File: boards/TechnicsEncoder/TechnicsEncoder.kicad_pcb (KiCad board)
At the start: 2 copper layers, 110.5 x 52.6 mm, 32 parts, among them J1 ISP, J2 Bender, J3 Technics, J4 SelectRX, J5 MIDI In, J6 MIDI Out, J7 BoardCon, J8 PistonEncoder, U1 ATmega48-20P, U2 6N137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

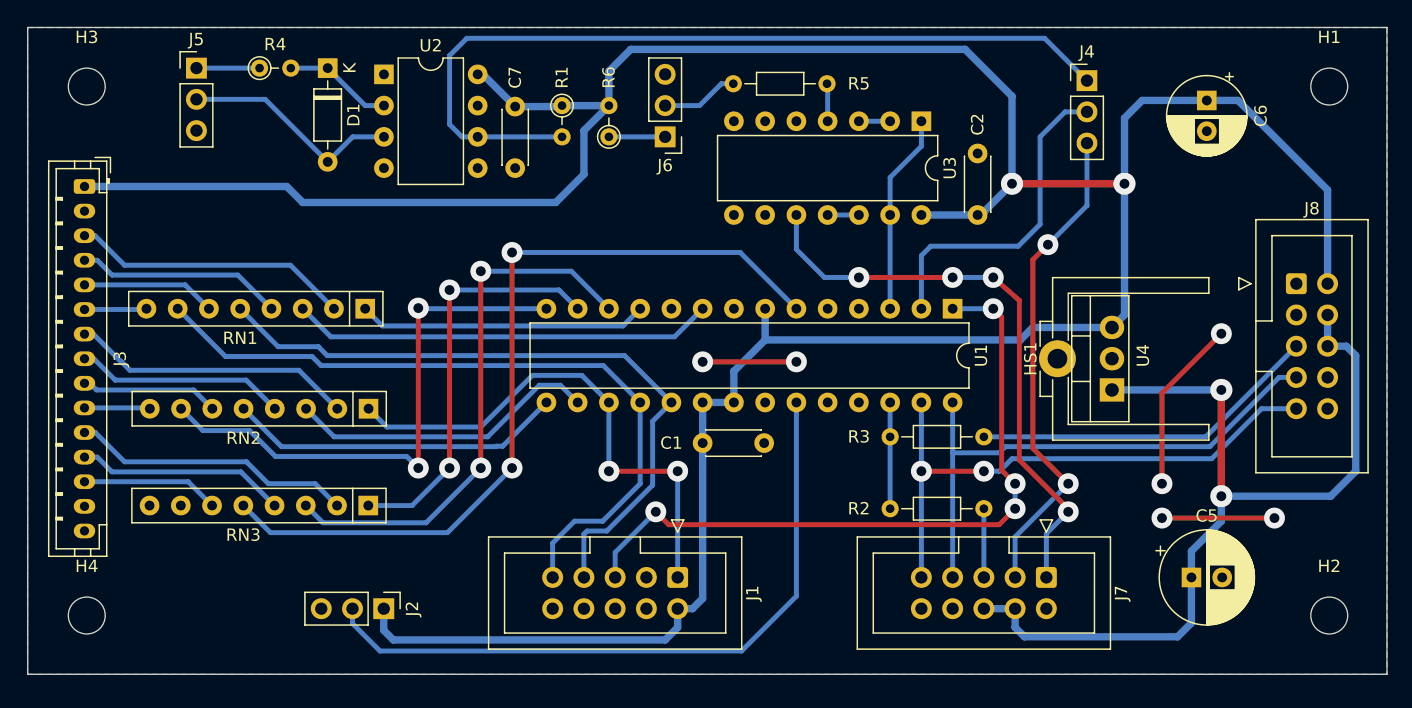
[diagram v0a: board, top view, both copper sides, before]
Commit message: Cleanup of PCB sizes and mounthole positions. Moved MIDI connectors to separate board.
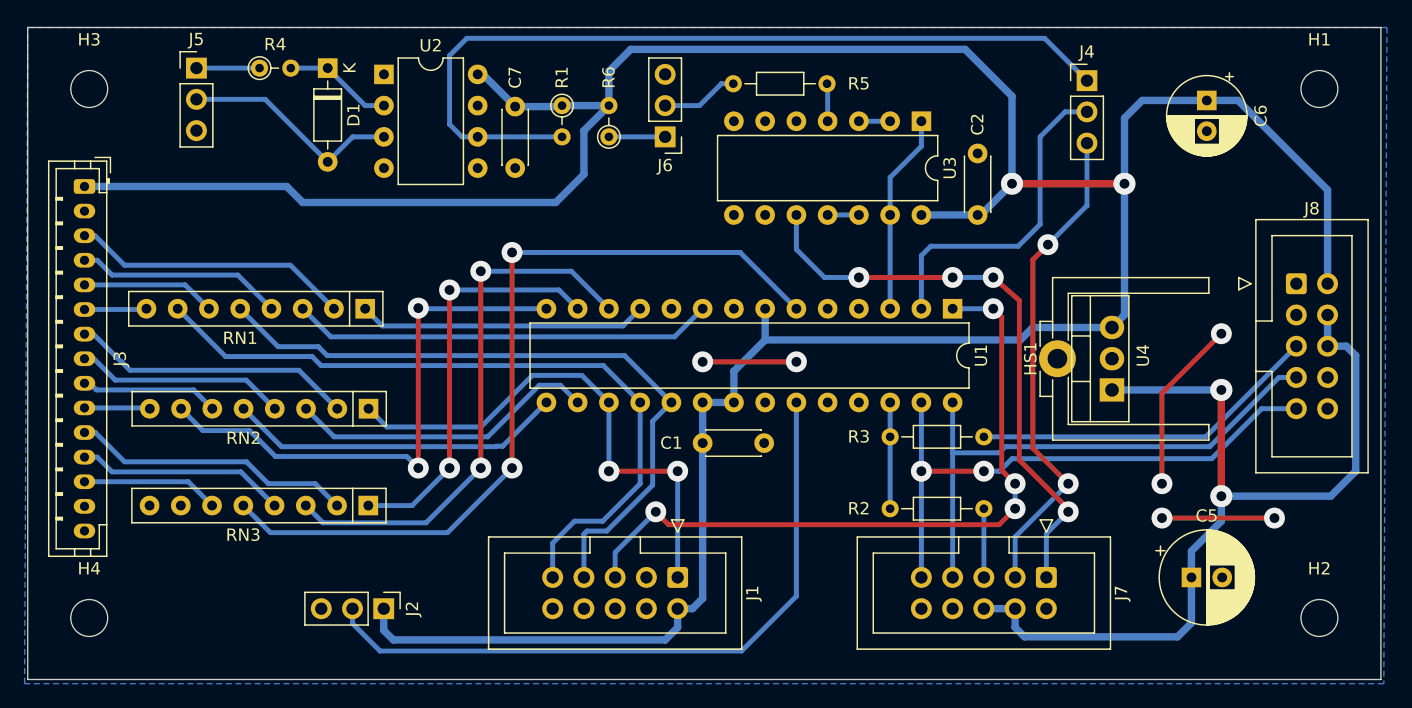
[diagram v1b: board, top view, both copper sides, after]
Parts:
- moved H1 0.82 mm to (180.9, 70.0)
- moved H2 0.82 mm to (180.9, 113.0)
- moved H3 0.28 mm to (80.9, 70.0)
- moved H4 0.28 mm to (80.9, 113.0)
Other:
- board size 110.5 x 52.6 mm -> 110 x 53 mm
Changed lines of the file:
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@@
 		(pad_to_mask_clearance 0)
 		(allow_soldermask_bridges_in_footprints no)
+		(aux_axis_origin 75.946 65.024)
 		(pcbplotparams
 			(layerselection 0x00010fc_ffffffff)
@@
 	(footprint "MountingHole:MountingHole_3mm"
 		(layer "F.Cu")
-		(at 181.746 112.824)
+		(at 180.946 113.024)
 		(descr "Mounting Hole 3mm, no annular")
 		(tags "mounting hole 3mm no annular")
@@
 	(footprint "MountingHole:MountingHole_3mm"
 		(layer "F.Cu")
-		(at 80.746 112.824)
+		(at 80.946 113.024)
 		(descr "Mounting Hole 3mm, no annular")
 		(tags "mounting hole 3mm no annular")
@@
 	(footprint "MountingHole:MountingHole_3mm"
 		(layer "F.Cu")
-		(at 80.746 69.824)
+		(at 80.946 70.024)
 		(descr "Mounting Hole 3mm, no annular")
 		(tags "mounting hole 3mm no annular")
@@
 	(footprint "MountingHole:MountingHole_3mm"
 		(layer "F.Cu")
-		(at 181.746 69.824)
+		(at 180.946 70.024)
 		(descr "Mounting Hole 3mm, no annular")
 		(tags "mounting hole 3mm no annular")
@@
 	(gr_rect
 		(start 75.946 65.024)
-		(end 186.436 117.602)
+		(end 185.946 118.024)
 		(stroke
 			(width 0.05)
@@
 		(layer "Cmts.User")
 		(pts
-			(xy 200.914 104.14) (xy 208.026 105.664)
+			(xy 80.946 70.024) (xy 75.946 65.024)
 		)
-		(height 0)
-		(orientation 0)
-		(gr_text "7,1120 mm"
-			(at 204.47 102.99 0)
-			(layer "Cmts.User")
-			(effects
-				(font
-					(size 1 1)
-					(thickness 0.15)
-				)
-			)
-		)
-		(format
-			(prefix "")
-			(suffix "")
-			(units 3)
-			(units_format 1)
-			(precision 4)
-		)
-		(style
-			(thickness 0.1)
-			(arrow_length 1.27)
-			(text_position_mode 0)
-			(extension_height 0.58642)
-			(extension_offset 0.5) keep_text_aligned)
-	)
-	(dimension
-		(type orthogonal)
-		(layer "Cmts.User")
-		(pts
-			(xy 80.746 112.824) (xy 80.746 69.824)
-		)
-		(height -8.102)
+		(height -12.366)
 		(orientation 1)
-		(gr_text "43,0000 mm"
-			(at 71.494 91.324 90)
+		(gr_text "5,0000 mm"
+			(at 67.43 67.524 90)
 			(layer "Cmts.User")
 			(effects
@@
 		(layer "Cmts.User")
 		(pts
-			(xy 75.946 65.024) (xy 80.746 69.824)
+			(xy 80.946 70.024) (xy 75.946 65.024)
 		)
-		(height -4.572)
+		(height -8.556)
 		(orientation 0)
-		(gr_text "4,8000 mm"
-			(at 78.346 59.302 0)
+		(gr_text "5,0000 mm"
+			(at 78.446 60.318 0)
 			(layer "Cmts.User")
 			(effects
@@
 		(layer "Cmts.User")
 		(pts
-			(xy 75.946 117.602) (xy 186.436 117.602)
+			(xy 80.946 113.024) (xy 180.946 113.024)
 		)
-		(height 6.858)
+		(height 12.198)
 		(orientation 0)
-		(gr_text "110,4900 mm"
-			(at 131.191 123.31 0)
+		(gr_text "100,0000 mm"
+			(at 130.946 124.072 0)
 			(layer "Cmts.User")
 			(effects
@@
 		(layer "Cmts.User")
 		(pts
-			(xy 80.746 112.824) (xy 75.946 117.602)
+			(xy 80.946 70.024) (xy 80.946 113.024)
 		)
-		(height -8.61)
+		(height -12.366)
 		(orientation 1)
-		(gr_text "4,7780 mm"
-			(at 70.986 115.213 90)
+		(gr_text "43,0000 mm"
+			(at 67.43 91.524 90)
 			(layer "Cmts.User")
 			(effects
@@
 		(layer "Cmts.User")
 		(pts
-			(xy 186.436 117.602) (xy 186.436 65.024)
+			(xy 75.946 65.024) (xy 185.946 65.024)
 		)
-		(height 7.366)
-		(orientation 1)
-		(gr_text "52,5780 mm"
-			(at 192.652 91.313 90)
+		(height -7.112)
+		(orientation 0)
+		(gr_text "110,0000 mm"
+			(at 130.946 56.762 0)
 			(layer "Cmts.User")
 			(effects
@@
 		(layer "Cmts.User")
 		(pts
-			(xy 75.946 65.024) (xy 80.746 69.824)
+			(xy 185.946 65.024) (xy 185.946 118.024)
 		)
-		(height -3.302)
+		(height 10.396)
 		(orientation 1)
-		(gr_text "4,8000 mm"
-			(at 71.494 67.424 90)
-			(layer "Cmts.User")
-			(effects
-				(font
-					(size 1 1)
-					(thickness 0.15)
-				)
-			)
-		)
-		(format
-			(prefix "")
-			(suffix "")
-			(units 3)
-			(units_format 1)
-			(precision 4)
-		)
-		(style
-			(thickness 0.1)
-			(arrow_length 1.27)
-			(text_position_mode 0)
-			(extension_height 0.58642)
-			(extension_offset 0.5) keep_text_aligned)
-	)
-	(dimension
-		(type orthogonal)
-		(layer "Cmts.User")
-		(pts
-			(xy 181.746 112.824) (xy 186.436 117.602)
-		)
-		(height 10.112)
-		(orientation 0)
-		(gr_text "4,6900 mm"
-			(at 184.091 121.786 0)
+		(gr_text "53,0000 mm"
+			(at 195.192 91.524 90)
 			(layer "Cmts.User")
 			(effects
@@
 		(polygon
 			(pts
-				(xy 75.946 65.024) (xy 186.436 65.024) (xy 186.436 117.602) (xy 75.946 117.602)
+				(xy 75.946 65.024) (xy 186.436 65.024) (xy 186.182 118.364) (xy 75.692 118.364)
 			)
 		)

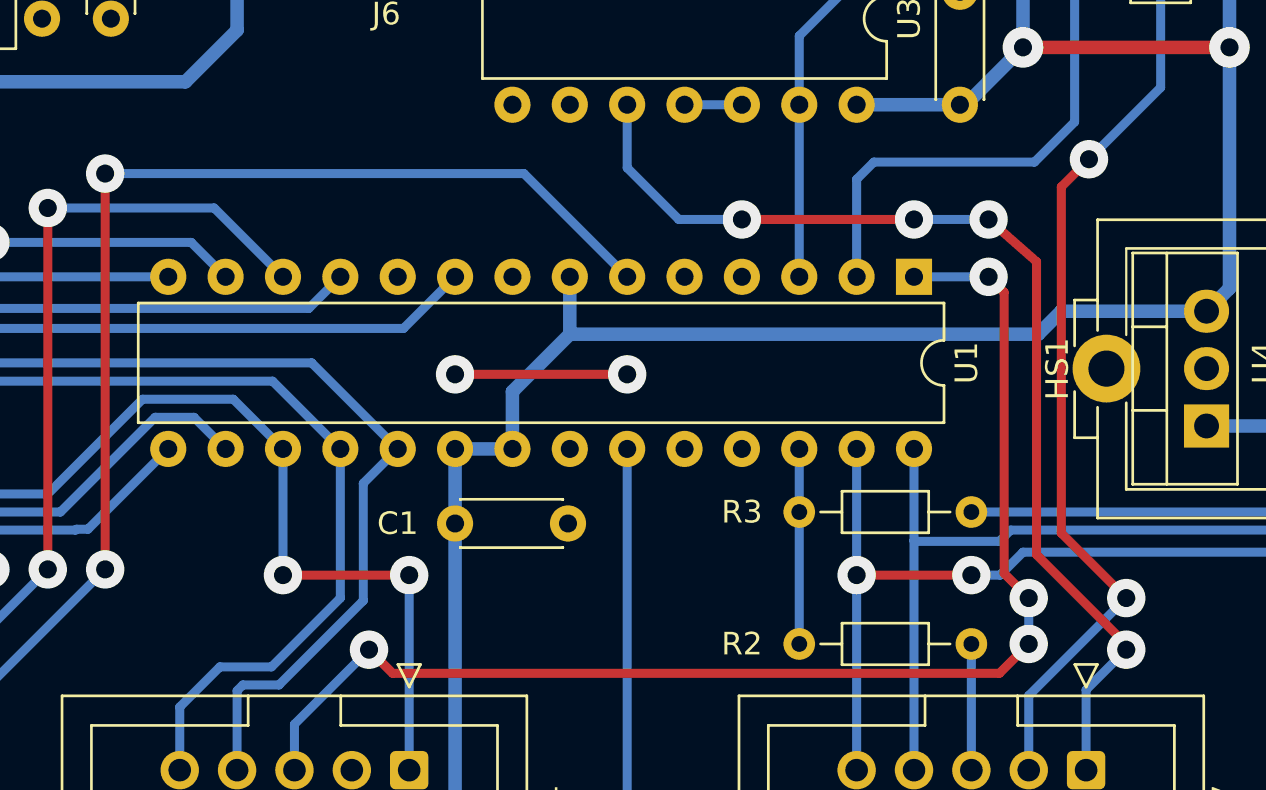
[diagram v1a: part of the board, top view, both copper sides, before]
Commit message: Added Optocoupler and RS232 converter to UART board lines.
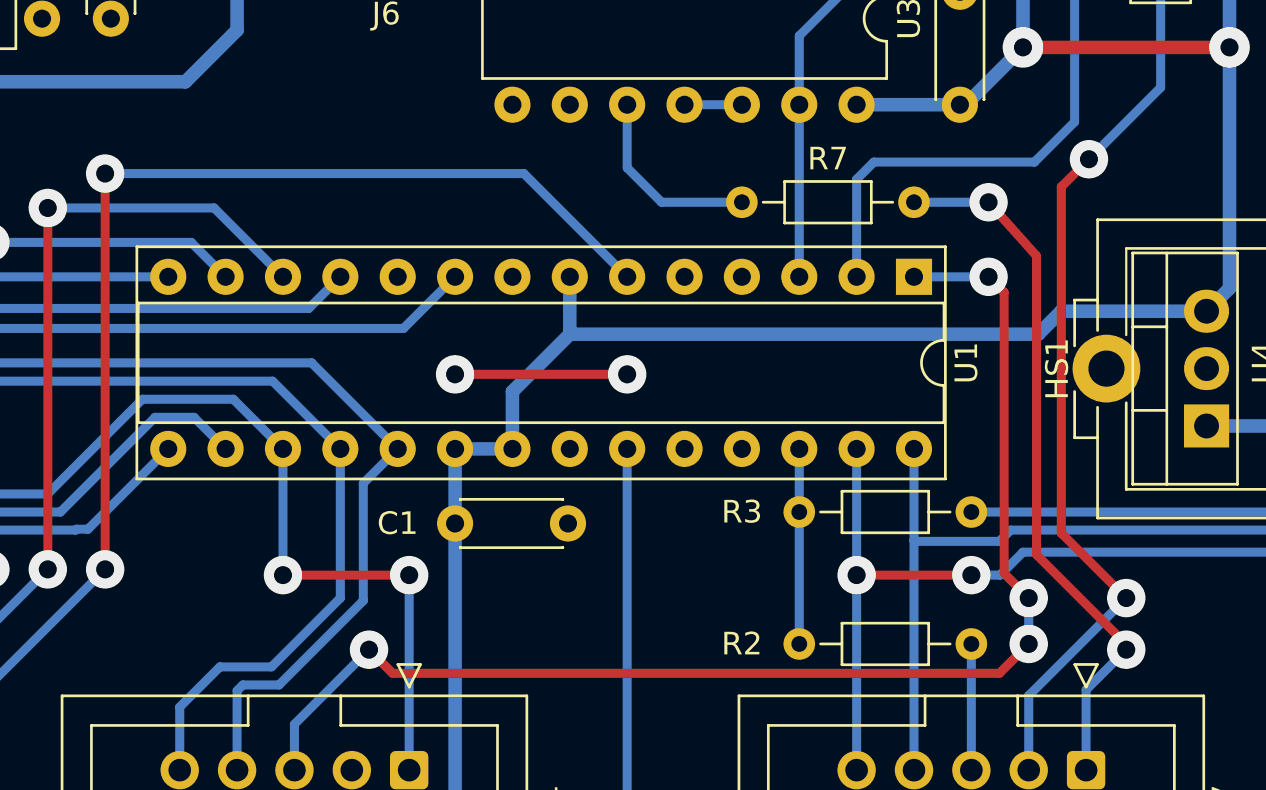
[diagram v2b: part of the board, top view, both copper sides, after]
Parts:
- added R7: 220, Resistor_THT:R_Axial_DIN0204_L3.6mm_D1.6mm_P7.62mm_Horizontal, F.Cu at (143.5, 84.6)
- U1: footprint Package_DIP:DIP-28_W7.62mm -> Package_DIP:DIP-28_W7.62mm_Socket
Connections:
- U3 pad 10: TXD_OUT -> Net-(R7-Pad1)
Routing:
- net TXD_OUT: track 47.5 -> 31.6 mm, vias 4 -> 2
- net Net-(R7-Pad1): track 0.00 -> 8.51 mm

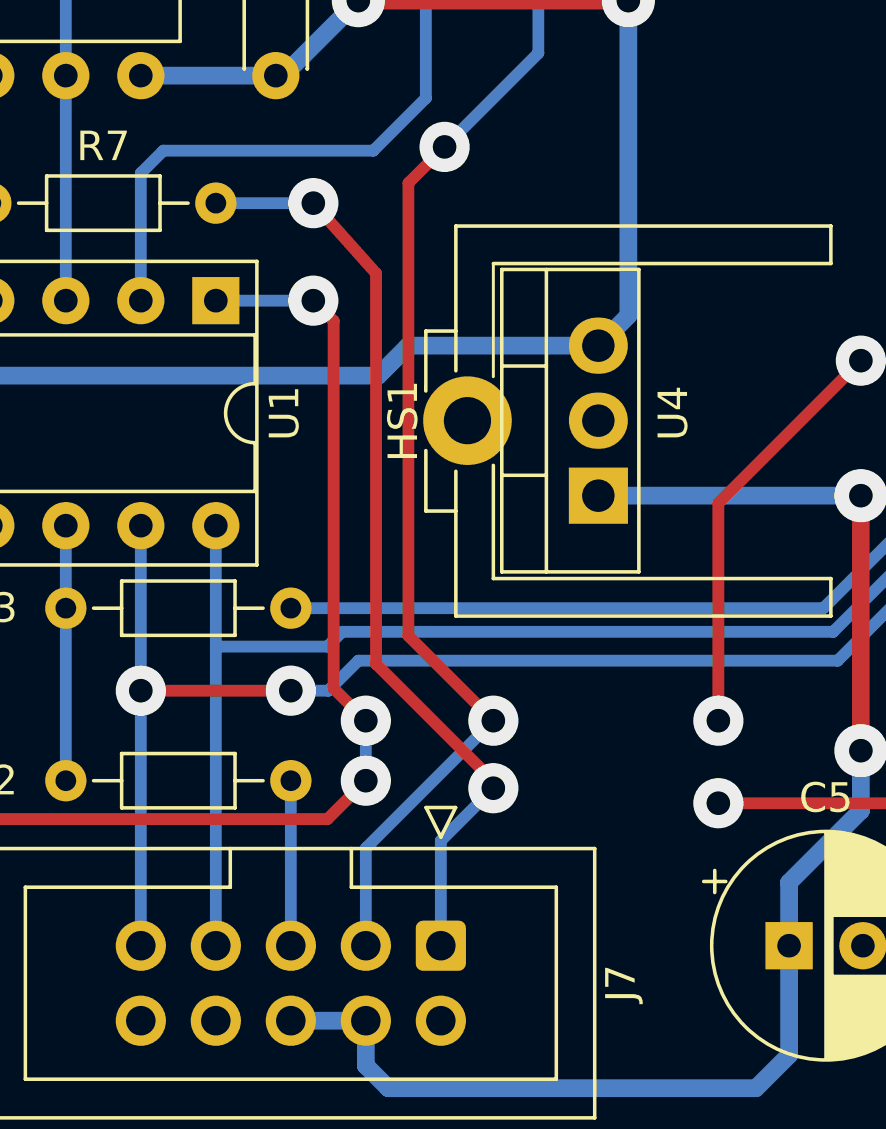
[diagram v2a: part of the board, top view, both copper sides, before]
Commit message: Finished IO-Board PCB, switched RX/TX of board connectors for better routing
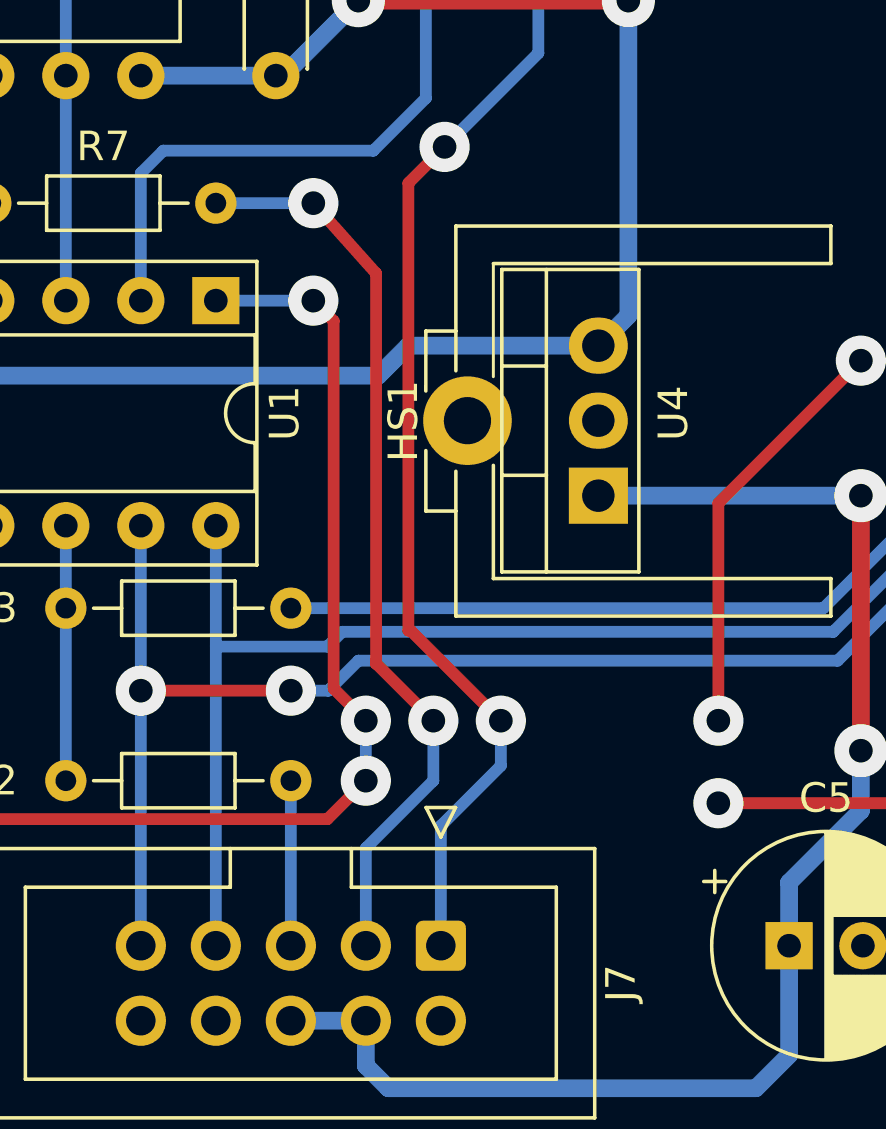
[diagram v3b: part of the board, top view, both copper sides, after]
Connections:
- J7 pad 1: TXD_OUT -> Net-(J4-Pin_3)
- J7 pad 3: Net-(J4-Pin_3) -> TXD_OUT
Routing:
- net Net-(J4-Pin_3): track 40.1 -> 39.3 mm
- net TXD_OUT: track 31.6 -> 31.1 mm
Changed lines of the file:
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@@
 			(remove_unused_layers no)
 			(roundrect_rratio 0.147059)
-			(net 37 "TXD_OUT")
+			(net 28 "Net-(J4-Pin_3)")
 			(pinfunction "Pin_1")
 			(pintype "passive")
@@
 			(layers "*.Cu" "*.Mask")
 			(remove_unused_layers no)
-			(net 28 "Net-(J4-Pin_3)")
+			(net 37 "TXD_OUT")
 			(pinfunction "Pin_3")
 			(pintype "passive")
@@
 	)
 	(segment
-		(start 157.6517 83.9023)
-		(end 157.6517 99.2317)
+		(start 157.734 99.06)
+		(end 157.6517 99.06)
+		(width 0.4)
+		(layer "F.Cu")
+		(net 28)
+	)
+	(segment
+		(start 160.782 102.108)
+		(end 157.734 99.06)
 		(width 0.4)
 		(layer "F.Cu")
@@
 	)
 	(segment
-		(start 157.6517 99.2317)
-		(end 160.528 102.108)
+		(start 157.6517 83.9023)
+		(end 157.6517 99.06)
 		(width 0.4)
 		(layer "F.Cu")
@@
 	)
 	(via
-		(at 160.528 102.108)
+		(at 160.782 102.108)
 		(size 1.7)
 		(drill 0.8)
@@
 	)
 	(segment
-		(start 156.21 109.728)
-		(end 156.21 106.426)
+		(start 162.052 79.502)
+		(end 162.052 74.422)
 		(width 0.4)
 		(layer "B.Cu")
@@
 	)
 	(segment
-		(start 162.052 79.502)
-		(end 162.052 74.422)
+		(start 158.877 82.677)
+		(end 162.052 79.502)
 		(width 0.4)
 		(layer "B.Cu")
@@
 	)
 	(segment
-		(start 158.877 82.677)
-		(end 162.052 79.502)
+		(start 160.782 102.108)
+		(end 160.782 103.632)
 		(width 0.4)
 		(layer "B.Cu")
@@
 	)
 	(segment
-		(start 156.21 106.426)
-		(end 160.528 102.108)
+		(start 160.782 103.632)
+		(end 158.75 105.664)
+		(width 0.4)
+		(layer "B.Cu")
+		(net 28)
+	)
+	(segment
+		(start 158.75 105.664)
+		(end 158.75 109.728)
 		(width 0.4)
 		(layer "B.Cu")
@@
 	)
 	(segment
-		(start 156.556 86.96)
+		(start 156.556 100.076)
 		(end 156.556 100.18661)
 		(width 0.4)
@@
 	)
 	(segment
+		(start 156.556 86.96)
+		(end 156.556 100.076)
+		(width 0.4)
+		(layer "F.Cu")
+		(net 37)
+	)
+	(segment
 		(start 154.432 84.582)
 		(end 156.556 86.96)
@@
 	)
 	(segment
-		(start 156.556 100.18661)
-		(end 160.528 104.15861)
+		(start 158.496 102.108)
+		(end 156.556 100.168)
 		(width 0.4)
 		(layer "F.Cu")
@@
 	)
 	(segment
-		(start 160.528 104.15861)
-		(end 160.528 104.394)
+		(start 156.556 100.168)
+		(end 156.556 100.076)
 		(width 0.4)
 		(layer "F.Cu")
@@
 	)
 	(via
-		(at 160.528 104.394)
+		(at 158.496 102.108)
 		(size 1.7)
 		(drill 0.8)
@@
 	)
 	(segment
-		(start 158.75 106.172)
-		(end 158.75 109.728)
+		(start 158.496 104.14)
+		(end 156.21 106.426)
 		(width 0.4)
 		(layer "B.Cu")
@@
 	)
 	(segment
-		(start 151.13 84.582)
-		(end 154.432 84.582)
+		(start 158.496 102.108)
+		(end 158.496 104.14)
 		(width 0.4)
 		(layer "B.Cu")
@@
 	)
 	(segment
-		(start 160.528 104.394)
-		(end 158.75 106.172)
+		(start 156.21 106.426)
+		(end 156.21 109.728)
+		(width 0.4)
+		(layer "B.Cu")
+		(net 37)
+	)
+	(segment
+		(start 151.13 84.582)
+		(end 154.432 84.582)
 		(width 0.4)
 		(layer "B.Cu")
